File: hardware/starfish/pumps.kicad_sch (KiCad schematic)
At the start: 7 parts, among them J1001 Pump, Q1001 PSMN011-30YLC

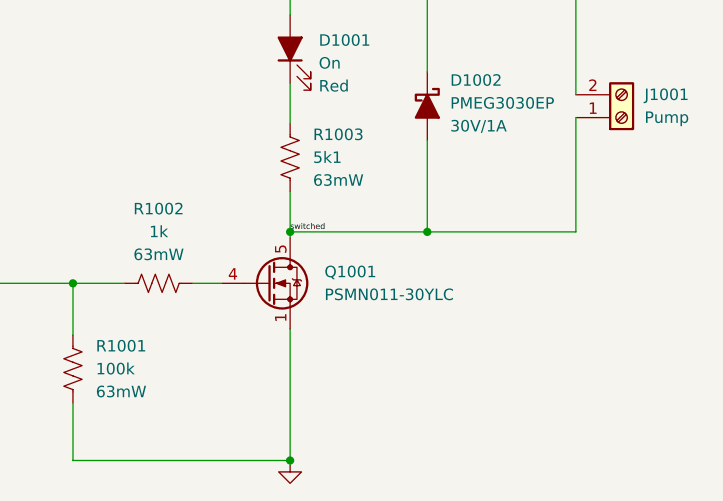
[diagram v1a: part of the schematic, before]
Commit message: starfish: update mosfet value and rating
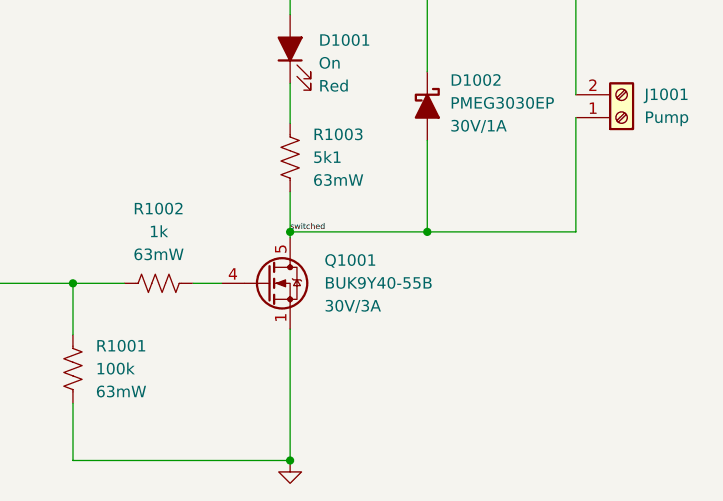
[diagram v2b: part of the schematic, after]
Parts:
- Q1001: value PSMN011-30YLC -> BUK9Y40-55B; Rating (none) -> 30V/3A
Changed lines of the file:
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@@
   (symbol (lib_id "Transistor_FET:PSMN5R2-60YL") (at 128.27 100.33 0) (unit 1)
     (in_bom yes) (on_board yes) (fields_autoplaced)
-    (property "Reference" "Q1001" (id 0) (at 134.62 99.0599 0)
+    (property "Reference" "Q1001" (id 0) (at 134.62 97.7899 0)
       (effects (font (size 1.27 1.27)) (justify left))
     )
-    (property "Value" "PSMN011-30YLC" (id 1) (at 134.62 101.5999 0)
+    (property "Value" "BUK9Y40-55B" (id 1) (at 134.62 100.3299 0)
       (effects (font (size 1.27 1.27)) (justify left))
     )
@@
       (effects (font (size 1.27 1.27)) hide)
     )
+    (property "Rating" "30V/3A" (id 5) (at 134.62 102.8699 0)
+      (effects (font (size 1.27 1.27)) (justify left))
+    )
     (pin "1")
